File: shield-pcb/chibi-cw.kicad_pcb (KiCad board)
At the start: 2 copper layers, 48.3 x 53.3 mm, 56 parts, among them J1 HEADPHONES, K1 CONN_3, K2 CONN_3, P1 CONN_4, P2 CONN_4, P3 CONN_2, Q1 BC847, U1 TPA6130A2

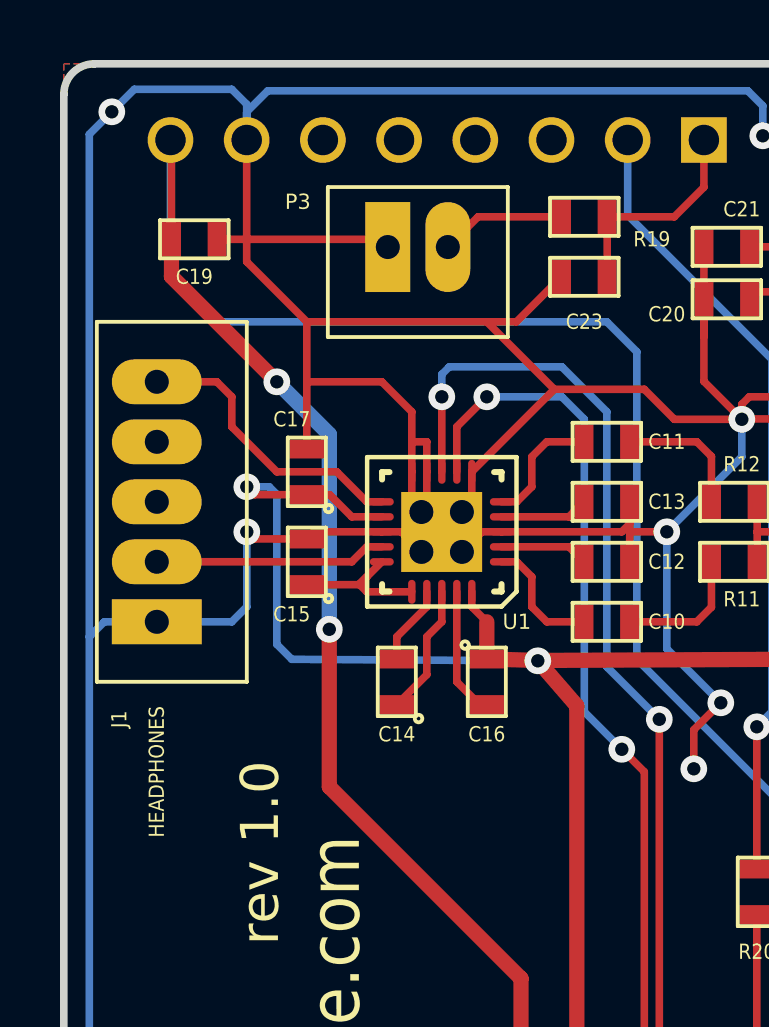
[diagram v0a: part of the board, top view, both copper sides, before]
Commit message: Added KEY silk label
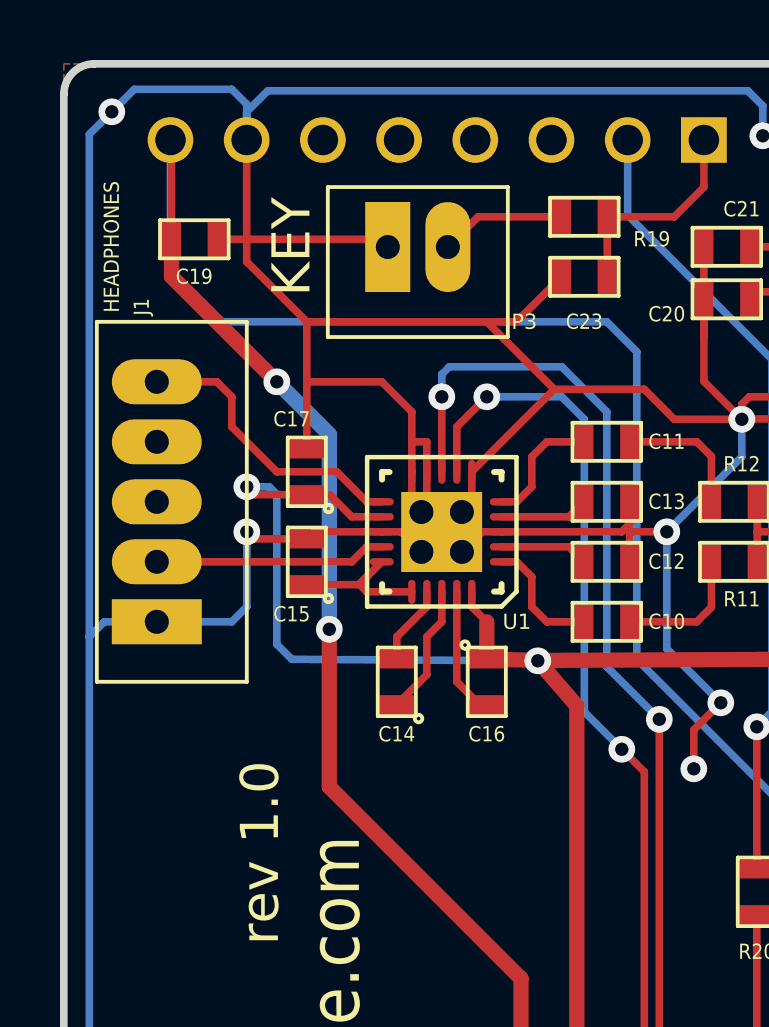
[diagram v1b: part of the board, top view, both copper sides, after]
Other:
- board text added: "KEY"
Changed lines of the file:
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@@
     (area 22.620525 22.5816 78.9184 81.9184)
     (thickness 1.6)
-    (drawings 31)
+    (drawings 32)
     (tracks 442)
     (zones 0)
@@
     (at 28.5 40 90)
     (descr "5pin 2mm pitch t-hole connector")
-    (fp_text reference J1 (at -7.25 -1.25 90) (layer F.SilkS)
+    (fp_text reference J1 (at 6.5 -0.5 90) (layer F.SilkS)
       (effects (font (size 0.508 0.4572) (thickness 0.1016)))
     )
-    (fp_text value HEADPHONES (at -9 0 90) (layer F.SilkS)
+    (fp_text value HEADPHONES (at 8.5 -1.5 90) (layer F.SilkS)
       (effects (font (size 0.508 0.4572) (thickness 0.1016)))
     )
@@
     (at 37.2 31.5)
     (descr "2pin 2mm pitch t-hole connector")
-    (fp_text reference P3 (at -4 -1.5) (layer F.SilkS)
+    (fp_text reference P3 (at 3.55 2.5) (layer F.SilkS)
       (effects (font (size 0.508 0.508) (thickness 0.1016)))
     )
@@
     )
   )
+  (gr_text KEY (at 33 31.5 90) (layer F.SilkS)
+    (effects (font (size 1.27 1.27) (thickness 0.3)))
+  )
   (gr_text OLED (at 61.25 69.25 90) (layer F.SilkS)

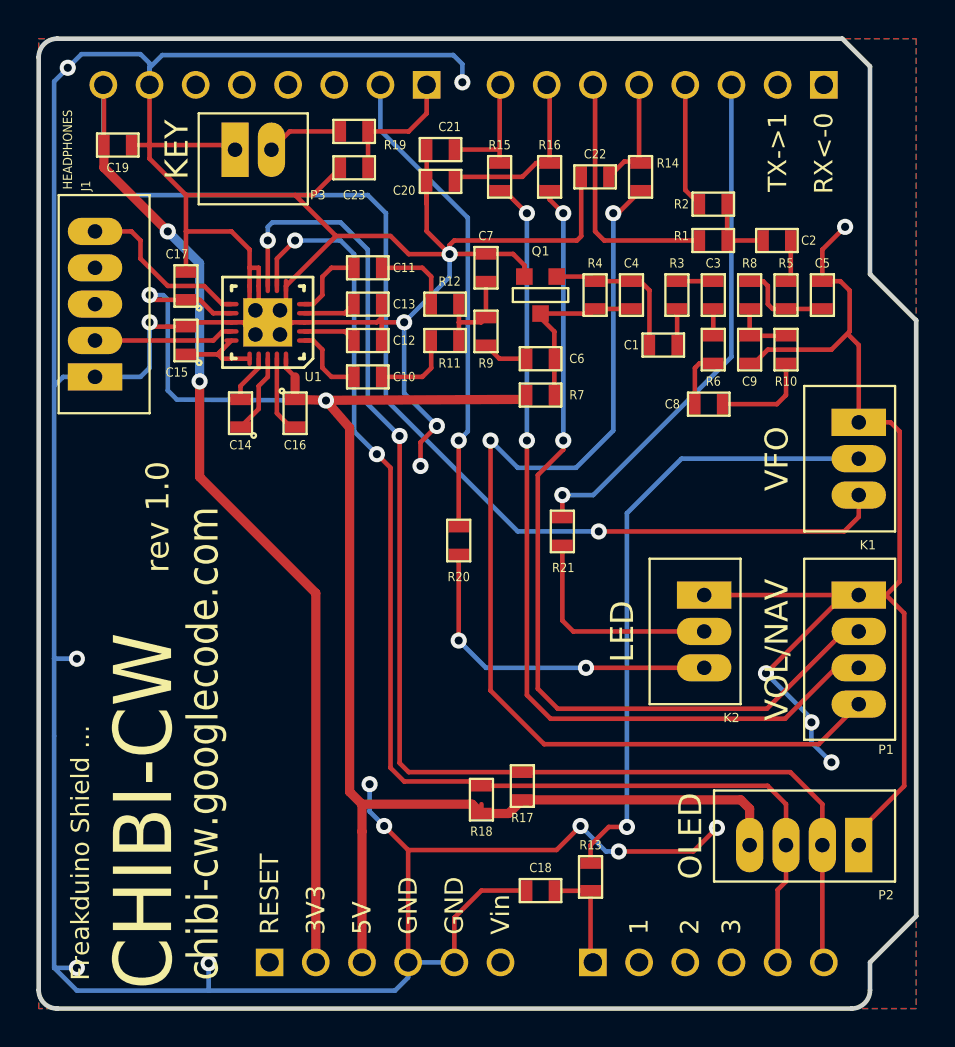
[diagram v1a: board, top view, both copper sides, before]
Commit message: 3D connector parts improved (more accurate size etc)
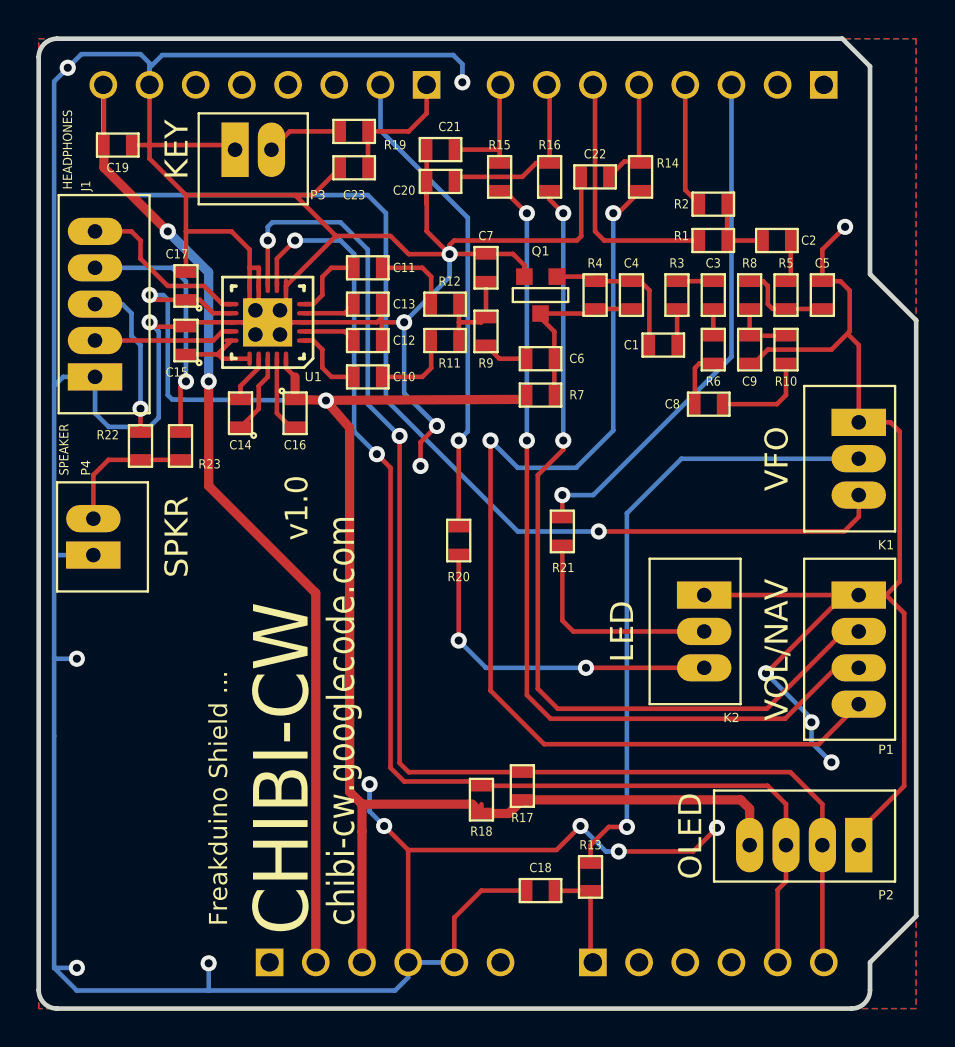
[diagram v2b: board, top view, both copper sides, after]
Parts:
- added P4: SPEAKER, CONN_2MM_2x1, F.Cu at (28.4, 52.8)
- added R22: 10R, SM0603, F.Cu at (31.0, 47.8)
- added R23: 10R, SM0603, F.Cu at (33.2, 47.8)
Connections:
- J1 pad 3: (no net) -> N-0000028
- J1 pad 4: (no net) -> N-0000027
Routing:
- net N-0000027: track 0.00 -> 13.7 mm, vias 0 -> 1
- net N-0000028: track 0.00 -> 8.95 mm, vias 0 -> 1
- net GND: track 329.2 -> 336.9 mm
- net N-0000026: track 0.00 -> 7.54 mm
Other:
- board text added: "SPKR"
- board text added: "v1.0"
- board text removed: "1"
- board text removed: "2"
- board text removed: "3"
- board text removed: "3V3"
- board text removed: "5V"
- board text removed: "GND"
- board text removed: "RESET"
- board text removed: "RX<-0"
- board text removed: "TX->1"
- board text removed: "Vin"
- board text removed: "rev 1.0"
